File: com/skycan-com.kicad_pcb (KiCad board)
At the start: 2 copper layers, 50 x 50 mm, 8 parts, among them J1 DF9_25P_1V_PLUG, J2 DF9_25P_1V_SOCKET, J3 DF9_25P_1V_PLUG, J4 DF9_25P_1V_SOCKET

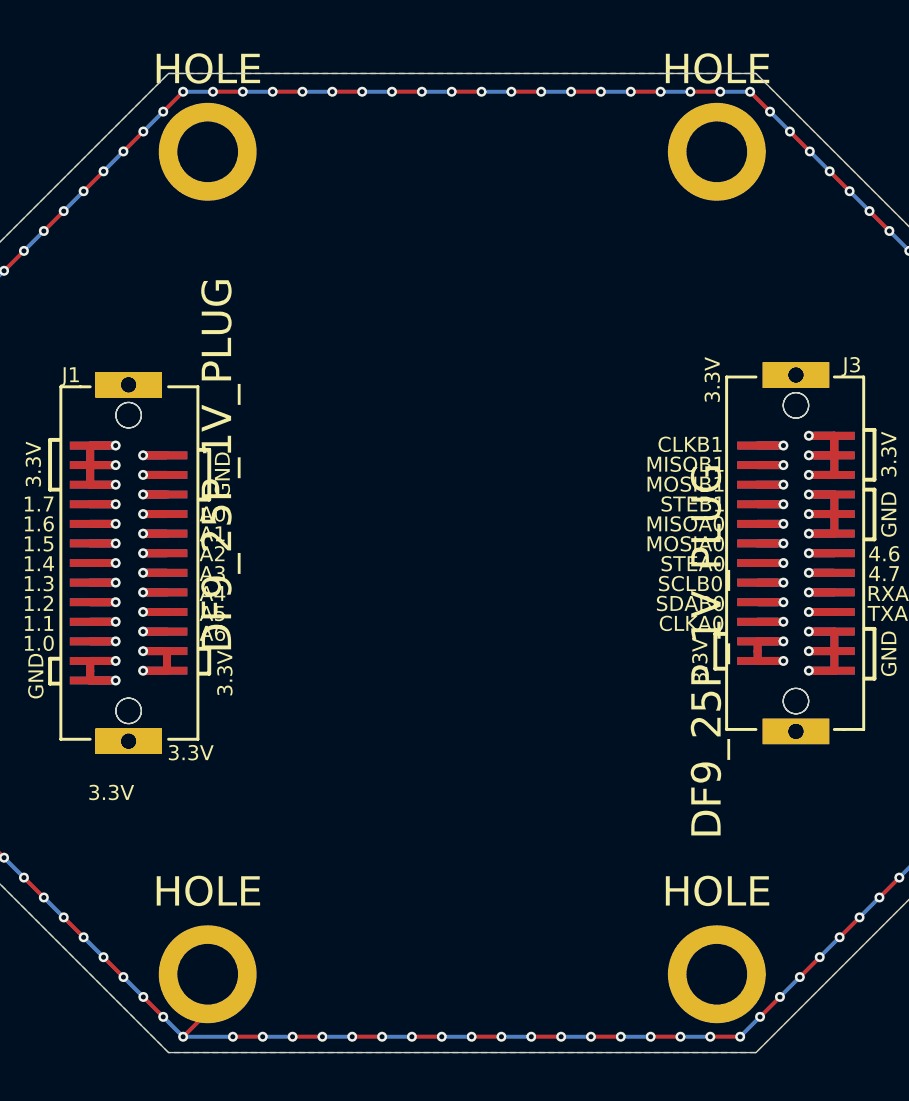
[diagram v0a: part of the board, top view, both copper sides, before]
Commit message: components placed to pcb
routing not yet started
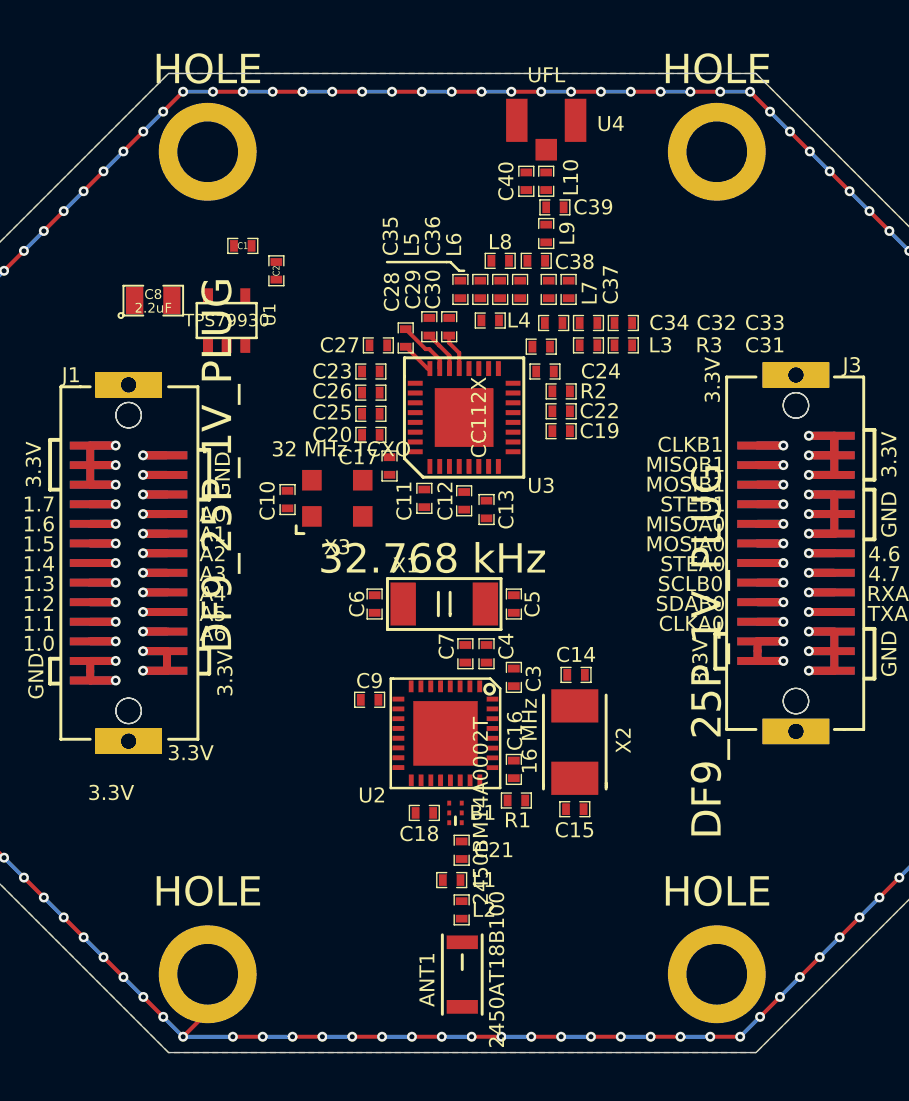
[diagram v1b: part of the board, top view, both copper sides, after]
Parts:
- added ANT1: 2450AT18B100, 2450AT18B100, F.Cu at (125.0, 136.0)
- added B1: 2450BM14A0002T, 2450BM14A0002, F.Cu at (124.7, 127.8)
- added C1: 100nF, SM0402_c, F.Cu at (113.8, 98.8)
- added C10: 100nF, SM0402_c, F.Cu at (116.1, 111.8)
- added C11: 47nF, SM0402_c, F.Cu at (123.1, 111.7)
- added C12: 47nF, SM0402_c, F.Cu at (125.1, 111.8)
- added C13: 220nF, SM0402_c, F.Cu at (126.2, 112.3)
- added C14: 18pF, SM0402_c, F.Cu at (130.8, 120.7)
- added C15: 18pF, SM0402_c, F.Cu at (130.7, 127.6)
- added C16: 1nF, SM0402_c, F.Cu at (127.6, 125.5)
- added C17: 22pF, SM0402_c, F.Cu at (121.3, 110.0)
- added C18: 2.2nF, SM0402_c, F.Cu at (123.1, 127.8)
- added C19: 47nF, SM0402_c, F.Cu at (130.0, 108.3)
- added C2: 10nF, SM0402_c, F.Cu at (115.5, 100.1)
- added C20: 47nF, SM0402_c, F.Cu at (120.3, 108.5)
- added C21: 1.2pF, SM0402_c, F.Cu at (125.0, 129.7)
- added C22: 47nF, SM0402_c, F.Cu at (130.0, 107.3)
- added C23: 47nF, SM0402_c, F.Cu at (120.3, 105.2)
- added C24: 47nF, SM0402_c, F.Cu at (129.2, 105.2)
- added C25: 47nF, SM0402_c, F.Cu at (120.3, 107.4)
- added C26: 47nF, SM0402_c, F.Cu at (120.3, 106.3)
- added C27: 47nF, SM0402_c, F.Cu at (120.7, 103.9)
- added C28: 1.8nF, SM0402_c, F.Cu at (122.1, 103.5)
- added C29: 47nF, SM0402_c, F.Cu at (123.3, 102.9)
- added C3: 100nF, SM0402_c, F.Cu at (127.6, 120.8)
- added C30: 10nF, SM0402_c, F.Cu at (124.3, 102.9)
- added C31: 10nF, SM0402_c, F.Cu at (133.2, 103.9)
- added C32: 56pF, SM0402_c, F.Cu at (131.4, 102.7)
- added C33: 100pF, SM0402_c, F.Cu at (133.2, 102.7)
- added C34: 39pF, SM0402_c, F.Cu at (129.7, 102.7)
- added C35: 5.1pF, SM0402_c, F.Cu at (124.9, 101.0)
- added C36: 5.1pF, SM0402_c, F.Cu at (126.9, 101.0)
- added C37: 2.2pF, SM0402_c, F.Cu at (130.4, 101.0)
- added C38: 5.1pF, SM0402_c, F.Cu at (128.8, 99.6)
- added C39: 6.2pF, SM0402_c, F.Cu at (129.7, 96.8)
- added C4: 100nF, SM0402_c, F.Cu at (126.2, 119.6)
- added C40: NA, SM0402_c, F.Cu at (128.3, 95.5)
- added C5: 12.5pF, SM0402_c, F.Cu at (127.6, 117.1)
- added C6: 12.5pF, SM0402_c, F.Cu at (120.5, 117.1)
- added C7: 100nF, SM0402_c, F.Cu at (125.2, 119.6)
- added C8: 2.2uF, SM0805, F.Cu at (109.2, 101.6)
- added C9: 100nF, SM0402_c, F.Cu at (120.3, 122.0)
- added L1: 2.7nH, SM0402, F.Cu at (124.5, 131.2)
- added L10: 22nH, SM0402, F.Cu at (129.3, 95.5)
- added L2: 3.3nH, SM0402, F.Cu at (125.0, 132.7)
- added L3: 56nH, SM0402, F.Cu at (129.0, 103.9)
- added L4: 56nH, SM0402, F.Cu at (126.4, 102.6)
- added L5: 27nH, SM0402, F.Cu at (125.9, 101.0)
- added L6: 27nH, SM0402, F.Cu at (128.0, 101.0)
- added L7: 15nH, SM0402, F.Cu at (129.4, 101.0)
- added L8: 15nH, SM0402, F.Cu at (126.9, 99.6)
- added L9: 43nH, SM0402, F.Cu at (129.3, 98.2)
- added R1: 22k, SM0402_r, F.Cu at (127.8, 127.1)
- added R2: 56k, SM0402_r, F.Cu at (130.0, 106.2)
- added R3: 18R, SM0402_r, F.Cu at (131.4, 103.9)
- added U1: TPS79930, SOT23-5, F.Cu at (113.0, 102.6)
- added U2: NRF8001, QFN32-5x5, F.Cu at (124.1, 123.7)
- added U3: CC112X, QFN32, F.Cu at (125.1, 107.6)
- added U4: UFL, UFL, F.Cu at (129.3, 92.4)
- added X1: 32.768 kHz, ABS10, F.Cu at (124.1, 117.1)
- added X2: 16 MHz, TXC-5X3_2, F.Cu at (130.7, 124.1)
- added X3: 32 MHz TCXO, WT325-3_2x2_5, F.Cu at (118.6, 111.7)
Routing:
- net N-000008: track 0.00 -> 2.84 mm
- net VDD: track 0.00 -> 2.11 mm
- net N-000006: track 0.00 -> 1.90 mm
- net N-000007: track 0.00 -> 1.70 mm

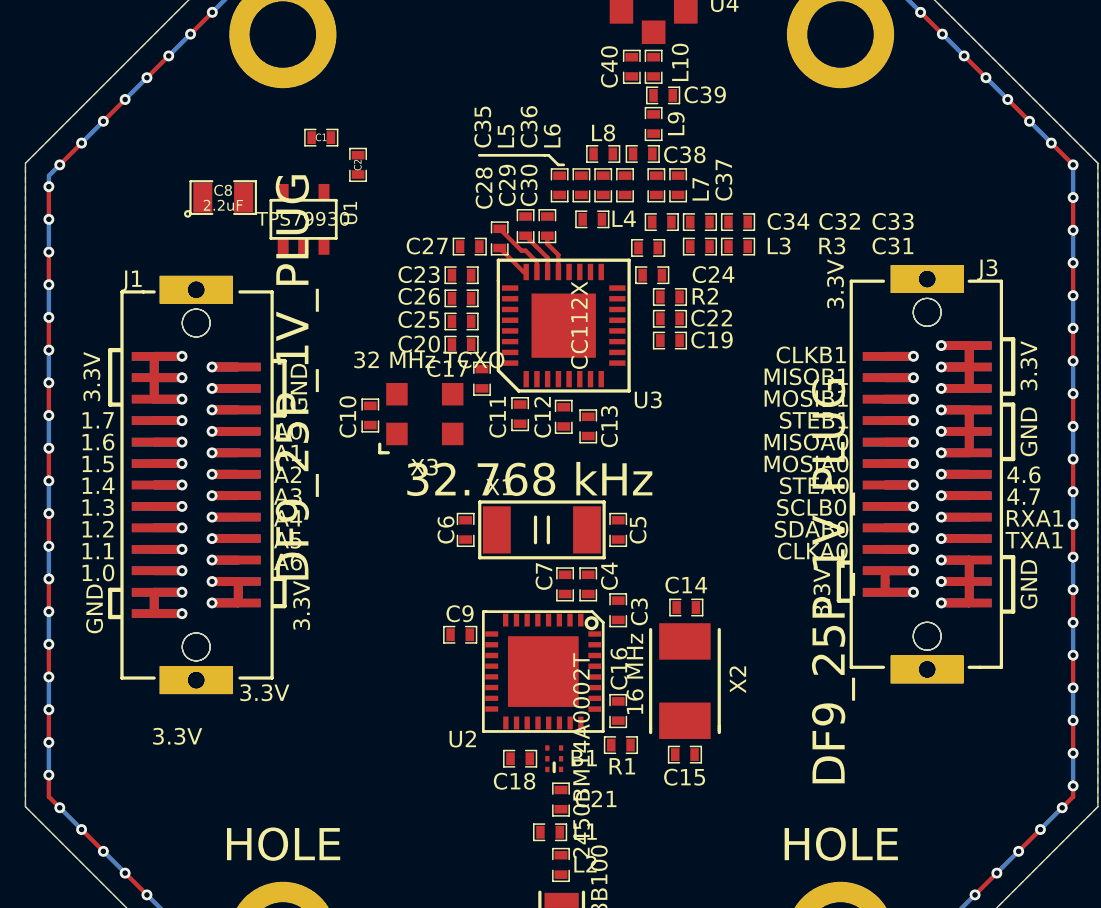
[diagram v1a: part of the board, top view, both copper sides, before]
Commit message: cc1120, nrf8001 digital stuff routed RF still to do
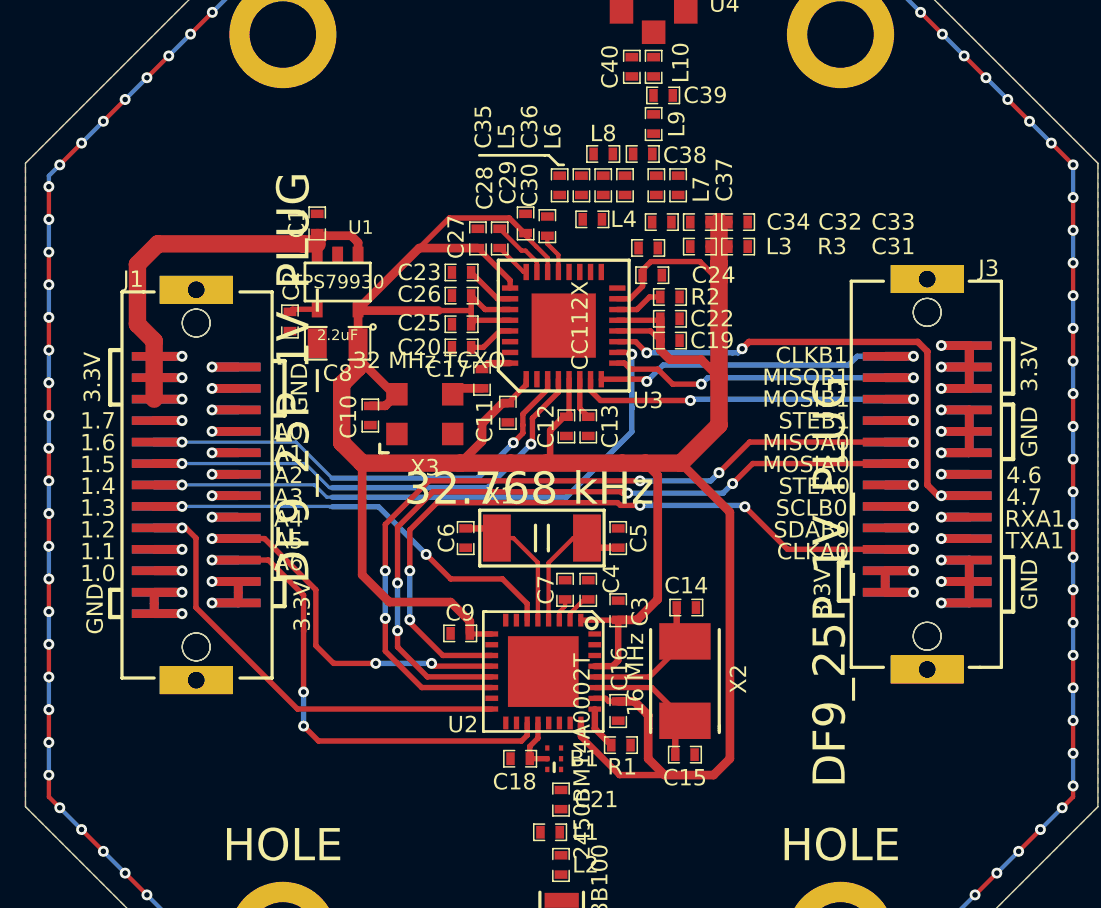
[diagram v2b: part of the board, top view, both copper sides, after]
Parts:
- moved C8 8.64 mm to (114.6, 108.4), turned to 180 degrees
- moved C2 7.96 mm to (112.3, 107.4), turned to 270 degrees
- moved C1 4.01 mm to (113.6, 102.8), turned to 90 degrees
- moved U1 3.32 mm to (114.6, 105.5), turned to 180 degrees
- moved C11 0.58 mm to (122.5, 111.6)
- moved C27 0.54 mm to (121.1, 103.5), turned to 90 degrees
- moved C12 0.46 mm to (125.2, 112.3)
- moved C5 0.38 mm to (127.6, 117.5)
- moved C6 0.38 mm to (120.5, 117.5)
- moved X1 0.38 mm to (124.1, 117.5)
- moved C4 0.25 mm to (126.2, 119.9)
- moved C7 0.25 mm to (125.2, 119.9)
- moved C26 0.13 mm to (120.3, 106.2)
- moved C20 0.13 mm to (120.3, 108.6)
- moved C23 0.13 mm to (120.3, 105.1)
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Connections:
- U2 pad 12: A6 -> A5
- U2 pad 16: P1.5 -> P1.2
- U2 pad 19: A5 -> A6
- U2 pad 6: P1.6 -> P1.3
- U3 pad 10: P1.2 -> P1.4
- U3 pad 3: P1.4 -> P1.6
- U3 pad 4: P1.3 -> P1.5
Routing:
- net VDD: track 2.11 -> 150.0 mm
- net SOMIA0: track 2.64 -> 39.1 mm, vias 1 -> 5
- net SIMOA0: track 2.64 -> 37.2 mm, vias 1 -> 5
- net CLKA0: track 2.64 -> 35.0 mm, vias 1 -> 5
- net P1.4: track 2.60 -> 29.4 mm, vias 1 -> 2
- net P4.7: track 2.60 -> 26.0 mm, vias 1 -> 3
- net A6: track 2.44 -> 23.7 mm, vias 1 -> 3
- net P1.5: track 2.60 -> 23.7 mm, vias 1 -> 2
- net P1.6: track 2.64 -> 23.1 mm, vias 1 -> 2
- net P1.2: track 2.60 -> 22.4 mm
- net +3.3V: track 41.0 -> 60.2 mm
- net P1.3: track 2.60 -> 21.4 mm, vias 1 -> 2
- net A5: track 2.44 -> 18.2 mm, vias 1 -> 3
- net SIMOB1: track 2.64 -> 17.1 mm, vias 1 -> 2
- net CLKB1: track 2.64 -> 16.4 mm, vias 1 -> 2
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
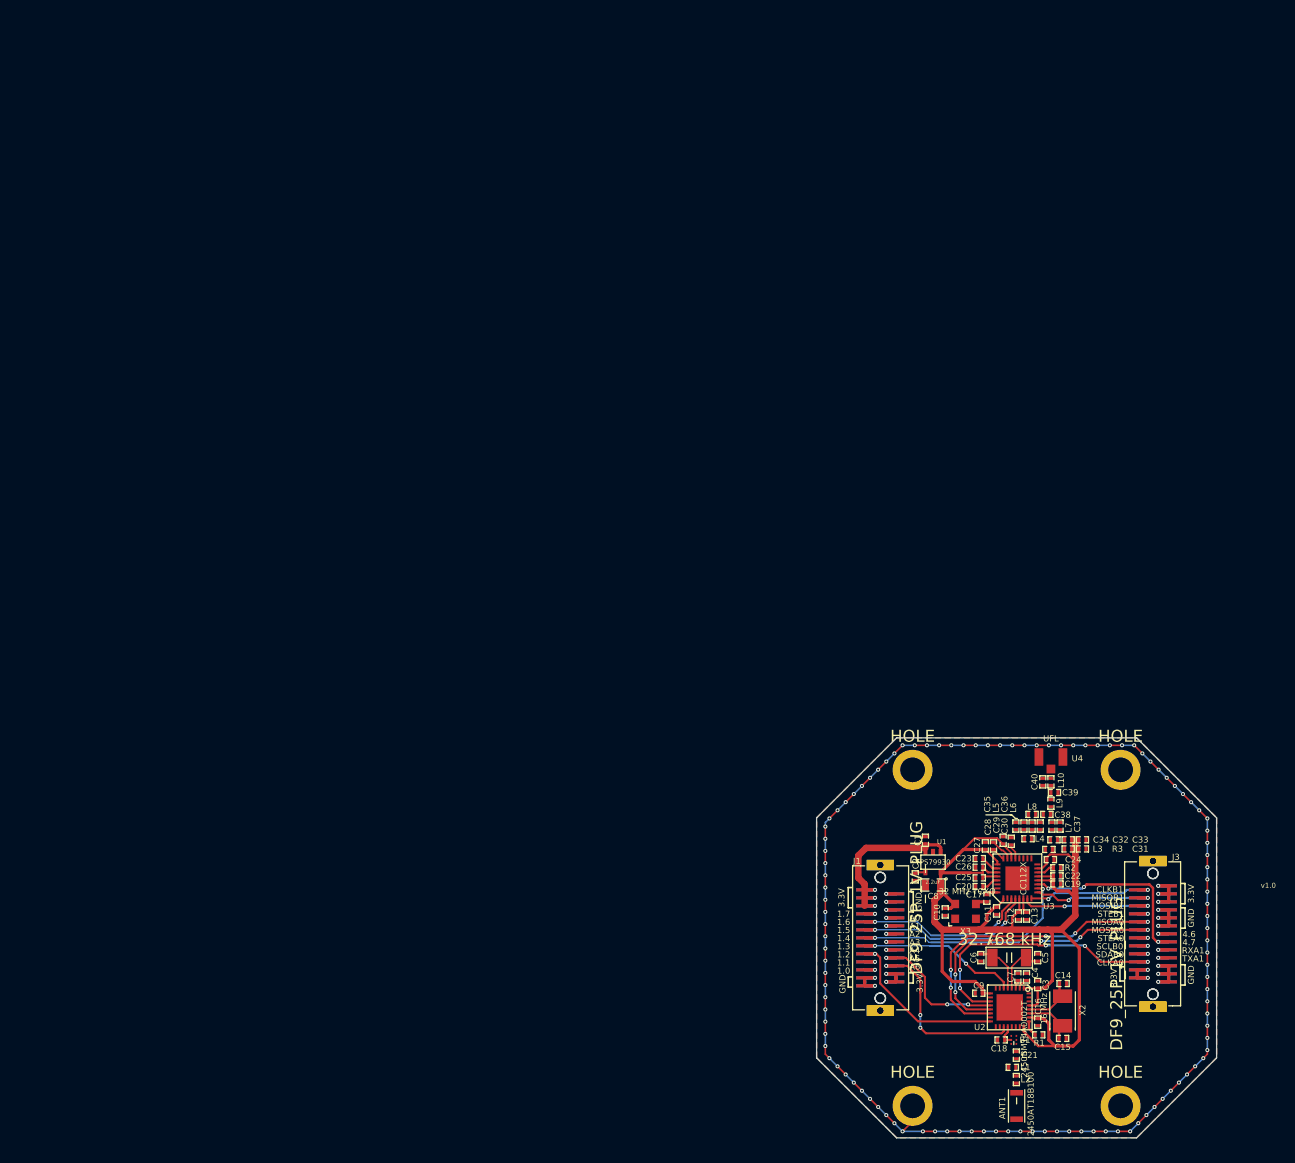
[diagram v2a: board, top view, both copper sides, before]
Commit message: com pcb routed and ground planes ready
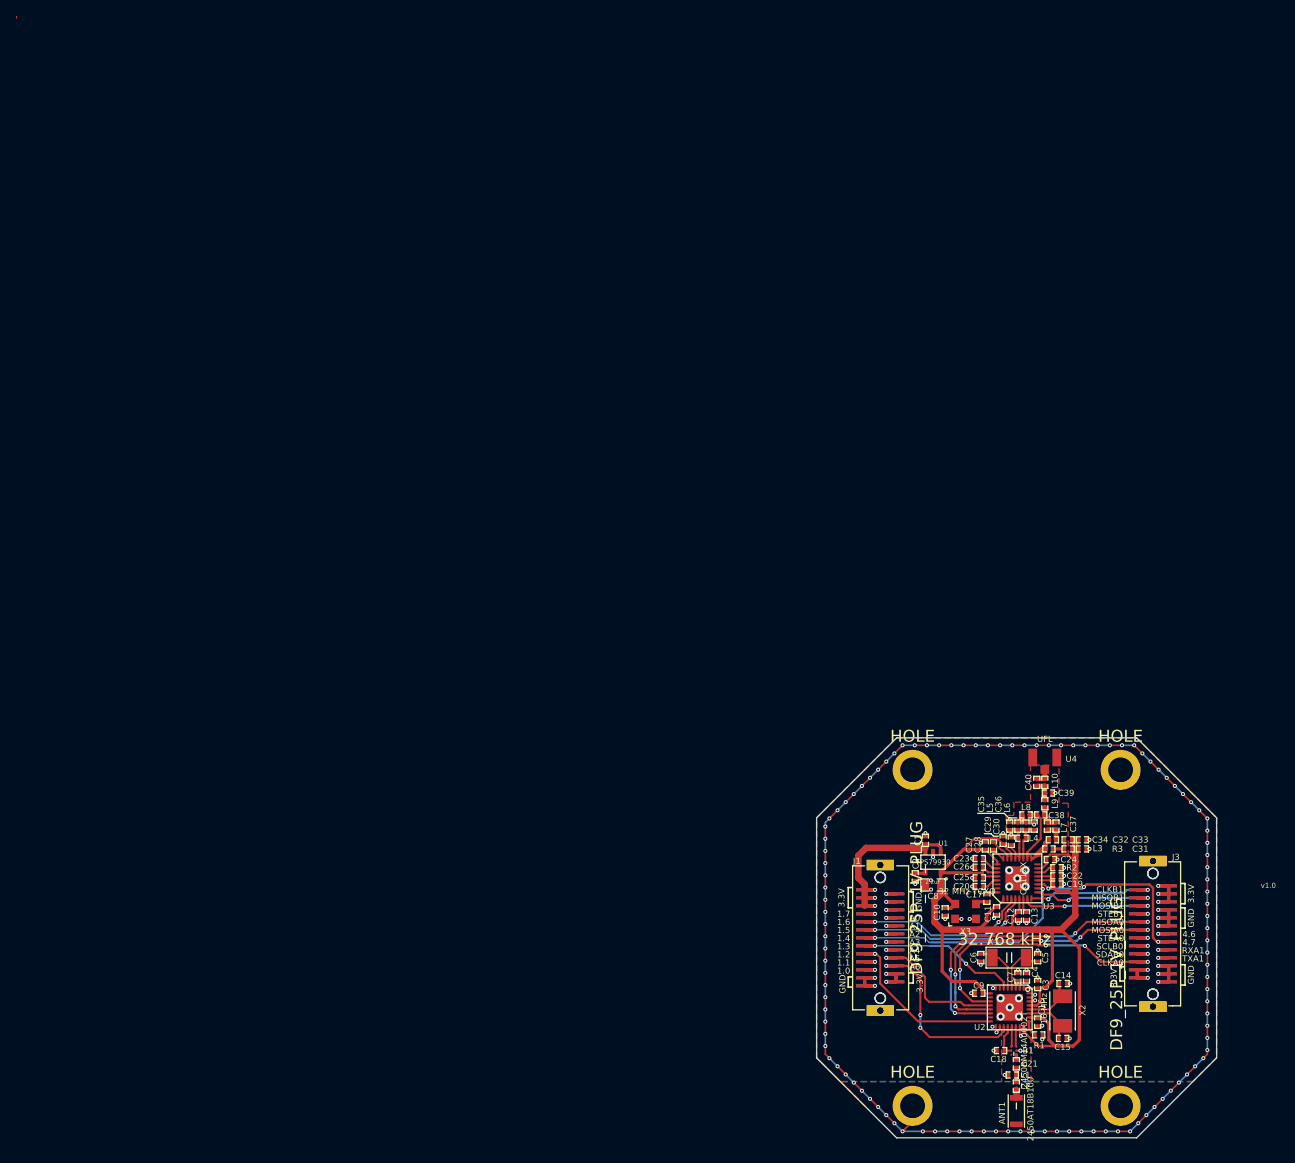
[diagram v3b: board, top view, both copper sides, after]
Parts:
- added STUB: VAL**, STUB, F.Cu at (0.00, 0.00)
- moved C18 1.34 mm to (123.0, 129.1)
- moved B1 1.33 mm to (124.7, 129.1)
- moved C21 1.08 mm to (125.0, 130.7)
- moved L1 0.95 mm to (124.5, 132.1)
- moved L2 0.83 mm to (125.0, 133.5)
- moved C40 0.76 mm to (127.5, 95.6)
- moved C38 0.76 mm to (128.0, 99.6)
- moved L4 0.76 mm to (125.7, 102.6)
- moved L8 0.76 mm to (126.2, 99.6)
- moved U4 0.76 mm to (128.5, 92.5)
- moved C39 0.76 mm to (129.0, 96.9)
- moved L10 0.76 mm to (128.5, 95.6)
- moved L9 0.76 mm to (128.5, 98.2)
- moved C35 0.76 mm to (124.1, 101.0)
- moved C36 0.76 mm to (126.2, 101.0)
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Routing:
- net GND: track 212.0 -> 261.2 mm, vias 124 -> 180
- net N-000002: track 0.00 -> 7.26 mm
- net N-0000069: track 0.00 -> 4.91 mm
- net N-0000070: track 0.00 -> 4.85 mm
- net N-0000012: track 0.00 -> 3.59 mm
- net N-0000068: track 0.00 -> 3.15 mm
- net N-0000013: track 0.00 -> 2.79 mm
- net N-0000014: track 0.00 -> 2.66 mm
- net N-0000032: track 0.00 -> 2.53 mm
- net N-0000030: track 0.00 -> 2.52 mm
- net N-000003: track 0.00 -> 2.35 mm
- net N-0000011: track 0.00 -> 2.18 mm
- net N-0000041: track 0.00 -> 1.94 mm
- net N-000001: track 0.00 -> 1.93 mm
- net N-0000047: track 2.64 -> 4.06 mm
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
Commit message: add com logo to pcb
only via stitching to do
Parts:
- added G***: OSHW-logo_silkscreen-front_20mm, OSHW-logo_silkscreen-front_20mm, B.Cu at (125.0, 115.0)
- added VAL: skycan-com-logo, skycan-com-logo, F.Cu at (139.6, 127.8)
